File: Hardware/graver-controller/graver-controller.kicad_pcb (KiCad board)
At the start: 2 copper layers, 110 x 70 mm, 117 parts, among them J101 DC jack 5.5x2.1, J201 Handpiece, J301 USB-C, J302 SWD, J401 LCD XH 1x7, J402 NMJ6HCD2, Q101 DMP6023LE, Q201 IRLR3410, Q202 SI2309CDS, Q203 BSS123, SW301 BOOT0, SW302 RESET, SW401 EC11E15244G1, U101 LM5164DDAR, U102 AP2112K-3.3, U201 UCC27517DBVR, U202 TLV9062IDR, U301 STM32F411CEU6, U302 USBLC6-2SC6, U401 PESD5V0S2BT, Y301 25MHz 10pF

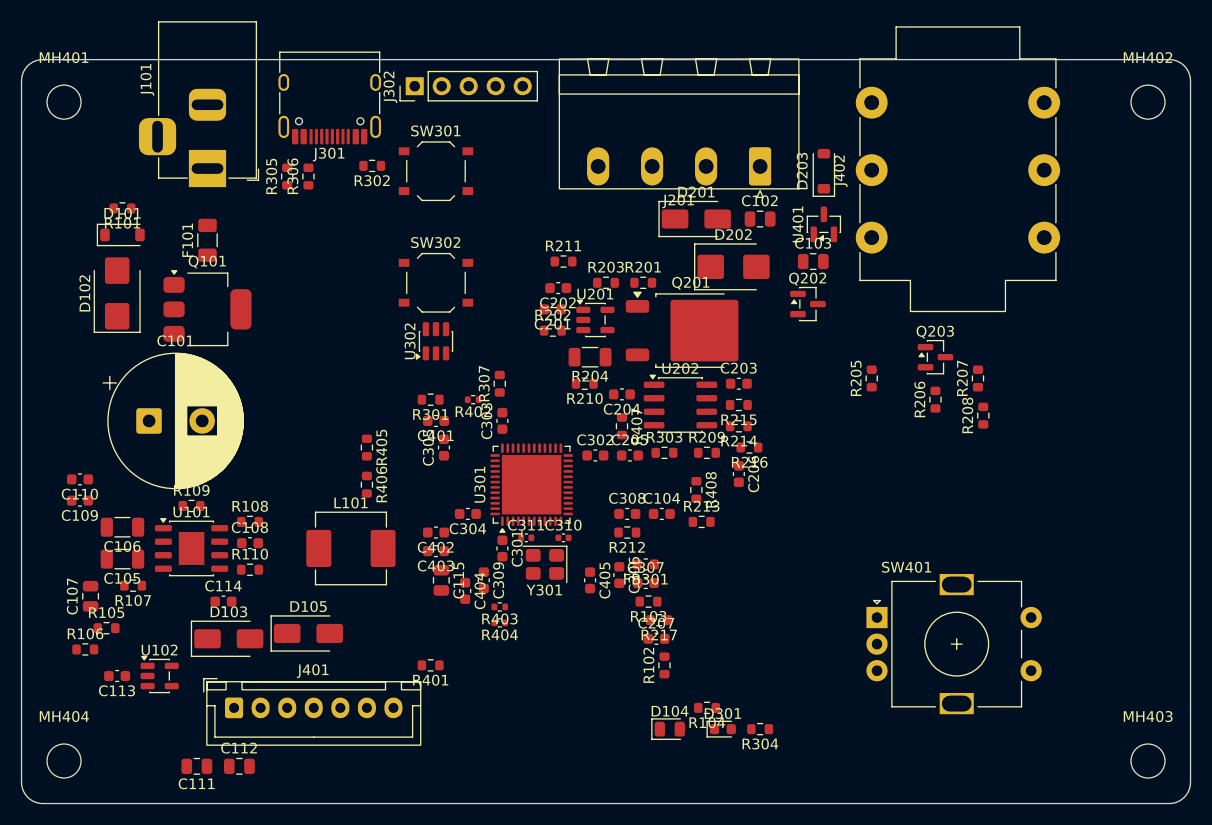
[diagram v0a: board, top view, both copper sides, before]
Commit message: hardware: copper script, first pass of the locked critical copper
tools/pcb/copper.py (place.py --copper): B.Cu ground pour, M3 and crystal
keepouts, QFN fanout with EP vias, decoupling links, crystal legs and
guard, VDDA chain, USB pair (39.8 / 39.0 mm, skew 0.8 mm, no vias),
VIN and flyback loop at 1.0 mm, buck loops, +5V / +3V3 links; all locked
and grouped. Repo board: 0 DRC errors, 0 parity, 107 pad pairs left for
the router. Known: NRST and the pedal inputs are trapped behind the
crystal island, R209/R213 are not at the shunt, 12 short local traces
not drawn; see README.
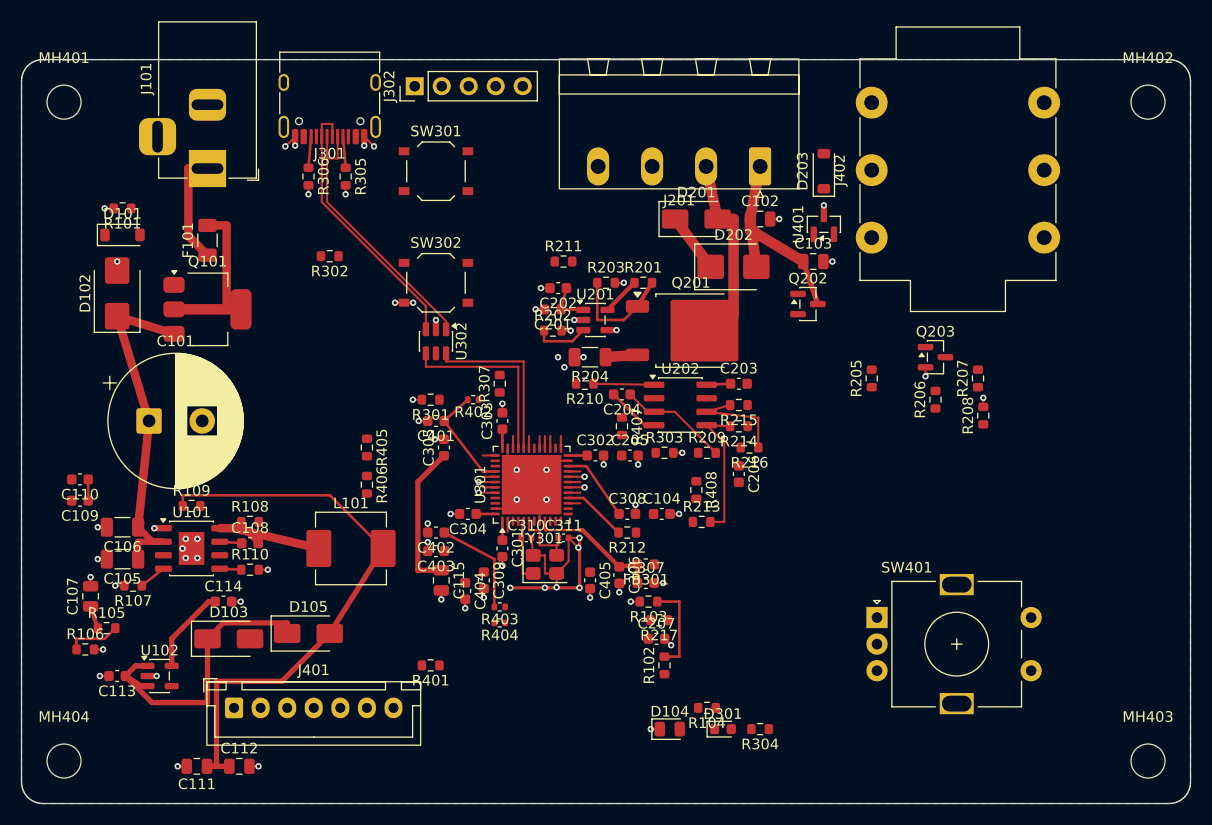
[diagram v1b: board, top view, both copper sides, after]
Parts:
- moved R302 9.39 mm to (79.0, 68.5)
- moved R305 5.50 mm to (80.5, 61.0), turned to -90 degrees
- moved C310 3.50 mm to (97.5, 95.0)
- moved C311 3.50 mm to (101.0, 95.0)
- turned R306 to -90 degrees
- turned U302 to -90 degrees
- turned Y301 to 0 degrees
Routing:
- net GND: track 0.00 -> 82.0 mm, vias 0 -> 74
- net VIN: track 0.00 -> 55.7 mm
- net Net-(D105-A): track 0.00 -> 54.9 mm
- net /MCU/USB_DP: track 0.00 -> 43.2 mm
- net /MCU/USB_DM: track 0.00 -> 42.0 mm
- net +5V: track 0.00 -> 32.9 mm
- net +3V3: track 0.00 -> 31.5 mm
- net Net-(Q101-D): track 0.00 -> 21.0 mm
- net /Driver/COIL_NEG: track 0.00 -> 15.6 mm
- net Net-(U101-SW): track 0.00 -> 13.8 mm
- net Net-(U202B-+): track 0.00 -> 13.3 mm
- net /MCU/VDDA: track 0.00 -> 12.7 mm
- net ENC_A: track 0.00 -> 11.3 mm
- net ENC_B: track 0.00 -> 11.0 mm
- net Net-(F101-Pad1): track 0.00 -> 10.7 mm
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- added copper zone on B.Cu, net GND

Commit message: hardware: copper pass 2, crystal in the corner, Kelvin taps at the shunt
Crystal island moved in front of pads 1-5 (PC13-15 unused): OSC legs
3.2 / 4.8 mm, pads 7-12 now escape freely, NRST cap 2.1 mm and VDDA 1 uF
2.5 mm from their pins. R209/R213 within 1.2 mm of the shunt pad edges,
Kelvin traces from the pad edges. Sense-side ground checked as a tree
with one tie at R204's ground pad, 5/5 pass. USB pair 37.9 / 37.9 mm,
skew 0. Repo board 0 DRC errors, 0 parity, 101 pad pairs left for the
router (was 107); strict routability test 6 open nets, 120 vias.
Known: VBAT decap 2.9 mm (advisory), R213 -> U202.5 and the buck
EN/UVLO divider left to the router, 12 local traces listed in README.
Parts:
- moved R405 31.3 mm to (113.5, 90.5)
- moved R406 31.3 mm to (113.5, 94.0)
- moved C110 27.0 mm to (82.5, 88.5), turned to 0 degrees
- moved C109 25.0 mm to (80.5, 90.5), turned to 0 degrees
- moved R211 21.1 mm to (109.0, 88.5), turned to -90 degrees
- moved R301 21.1 mm to (87.0, 103.0)
- moved R403 17.6 mm to (90.5, 84.5)
- moved R213 16.1 mm to (103.5, 81.2), turned to -90 degrees
- moved C205 15.8 mm to (104.2, 102.8)
- moved C207 14.0 mm to (105.2, 91.2)
- moved C311 11.1 mm to (94.9, 104.2), turned to -90 degrees
- moved R109 11.0 mm to (73.0, 100.5), turned to 180 degrees
- moved R209 10.7 mm to (106.0, 80.5)
- moved C404 8.96 mm to (100.0, 103.5)
- moved C402 8.49 mm to (87.0, 86.2)
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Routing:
- net GND: track 82.0 -> 119.1 mm, vias 74 -> 73
- net Net-(U202A--): track 0.00 -> 14.8 mm
- net Net-(U202B-+): track 13.3 -> 2.20 mm
- net Net-(D105-A): track 54.9 -> 44.1 mm
- net /Driver/OC_REF: track 9.97 -> 19.2 mm
- net /MCU/VDDA: track 12.7 -> 3.73 mm
- net VIN_SENSE: track 10.2 -> 1.55 mm
- net Net-(U301-VCAP1): track 7.16 -> 0.00 mm
- net ENC_A: track 11.3 -> 4.13 mm
- net ENC_B: track 11.0 -> 3.97 mm
- net I_SENSE: track 7.22 -> 1.15 mm
- net Net-(U301-PA10): track 1.15 -> 7.14 mm
- net LED_STAT: track 1.00 -> 6.56 mm, vias 0 -> 1
- net /Driver/SHUNT_HI: track 3.01 -> 8.35 mm
- net +3V3: track 31.5 -> 28.0 mm
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
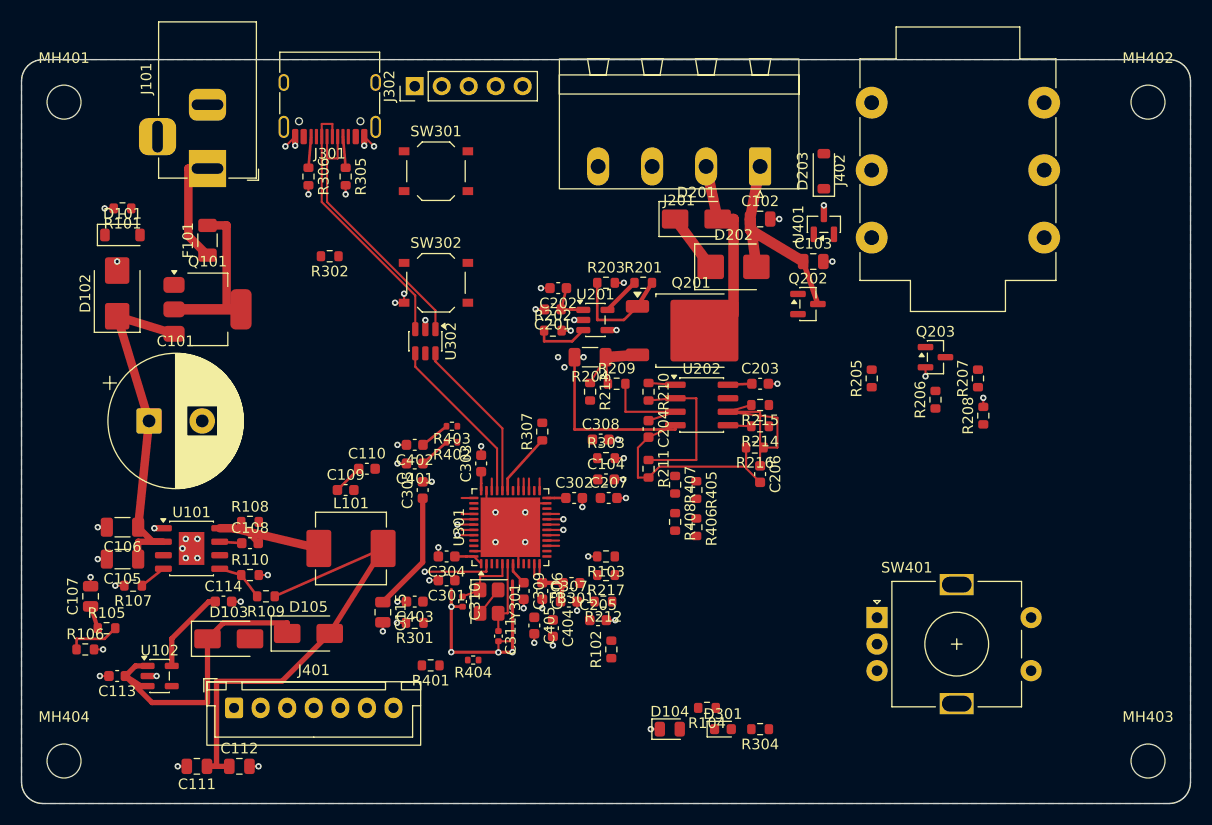
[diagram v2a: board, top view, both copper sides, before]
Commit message: hardware: scripted silkscreen
tools/pcb/silk.py (place.py --copper --silk): references at 1.0 mm /
0.15 mm placed by search next to their part, off pads and off each
other (10 inside the body, 87 within 1.5 mm, 7 within 3 mm, 9 in
reference rows); rear-edge labels DC 24V, USB, SWD, HANDPIECE with the
pins in board order (4 GND 3 NTC 2 COIL 1 VIN), PEDAL; J401 pin names;
pin-1 marks on J201, J302, J401; title. Library silk of the four rear
connectors clipped to the outline (4 lib_footprint_mismatch warnings,
deliberate). silk_overlap / silk_over_copper / silk_edge_clearance
92 / 92 / 17 -> 0. Copper unchanged (234 tracks, 78 vias, 6 zones),
0 DRC errors, 0 parity, 101 pad pairs left for the router.
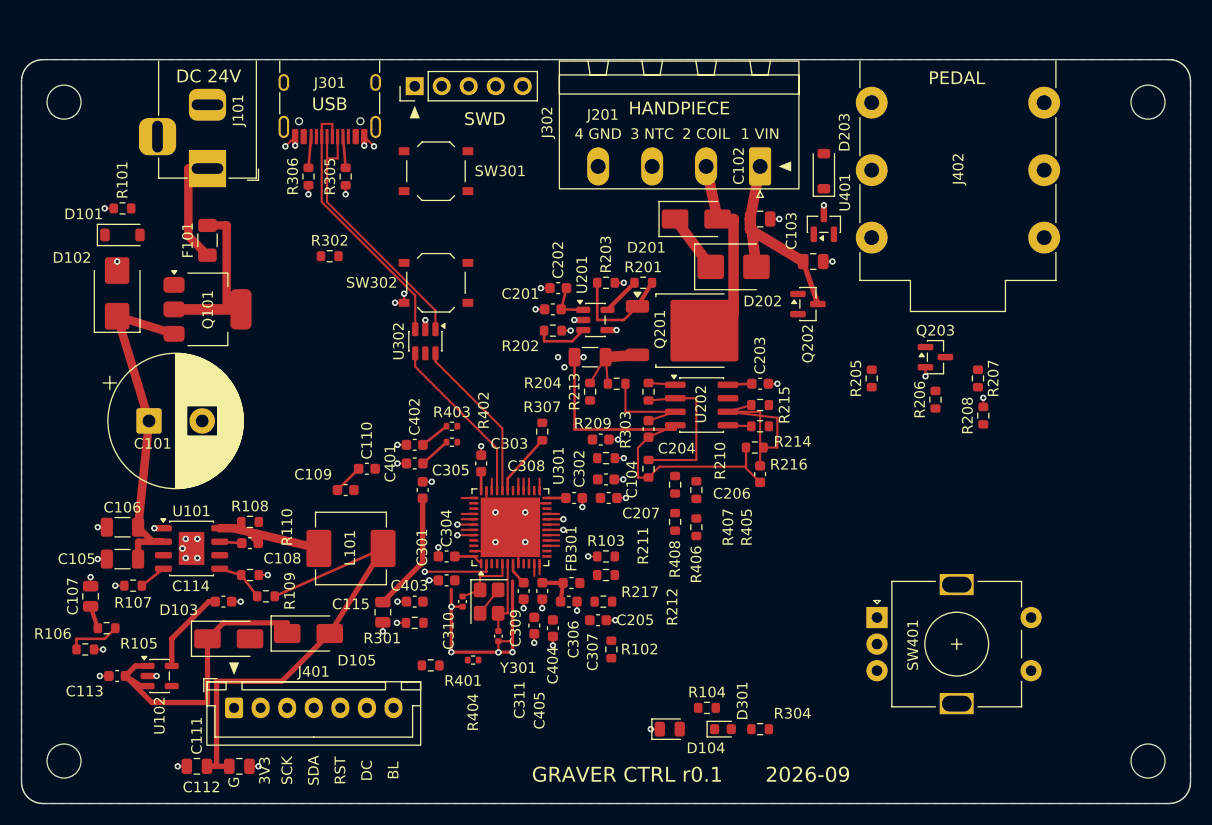
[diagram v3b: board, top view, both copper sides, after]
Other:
- board text added: "1 VIN"
- board text added: "2 COIL"
- board text added: "2026-09"
- board text added: "3 NTC"
- board text added: "3V3"
- board text added: "4 GND"
- board text added: "BL"
- board text added: "DC"
- board text added: "DC 24V"
- board text added: "G"
- board text added: "GRAVER CTRL r0.1"
- board text added: "HANDPIECE"
- board text added: "PEDAL"
- board text added: "RST"
- board text added: "SCK"
- board text added: "SDA"
- board text added: "SWD"
- board text added: "USB"

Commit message: hardware: autoroute stage for the remaining nets, first mostly routed board
tools/pcb/autoroute.py (place.py --route): copies the board to scratch,
runs KiCadRoutingTools with escalation off and strict sizes, grades the
copy with kicad-cli against the committed .kicad_pro and imports only
complete, error-free nets, grouped 'autorouted' so the stage can redo
them; zones refilled in pcbnew afterwards. copper.py reserves bands
along the USB pair on B.Cu after the router cut its ground reference
11 times. Scripted copper unchanged (234 tracks, 78 vias, flyback
20.3 mm, USB 37.88/37.88, Kelvin 1.15/1.23, sense ground 5/5).

Repo board: 0 DRC errors, 0 parity, 20 unconnected pad pairs in this
regeneration (the worker's run reached 13: the router is not
deterministic between runs). Left open: NTC, ENC_SW, ENC_B, +5V,
LCD_RST at the QFN (fanout stubs and vias boxing each other in at
0.5 mm pitch), the USBLC6 duplicate I/O pins (need two short bridges),
the encoder's two MP lugs. Ugly: +3V3 runs 229 mm, CLAMP tap 50 mm
around the DPAK.
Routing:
- net +3V3: track 28.0 -> 226.1 mm, vias 0 -> 17
- net VIN: track 55.7 -> 198.0 mm, vias 0 -> 2
- net VBUS: track 0.00 -> 74.6 mm, vias 0 -> 6
- net ENC_A: track 4.13 -> 72.2 mm, vias 0 -> 5
- net /Driver/CLAMP: track 5.61 -> 73.5 mm, vias 0 -> 2
- net SWDIO: track 1.15 -> 64.0 mm, vias 0 -> 2
- net NRST: track 2.18 -> 58.1 mm, vias 0 -> 4
- net LED_STAT: track 6.56 -> 54.3 mm, vias 1 -> 6
- net Net-(U301-BOOT0): track 1.55 -> 47.1 mm, vias 1 -> 3
- net LCD_DC: track 1.15 -> 46.4 mm, vias 0 -> 4
- net Net-(D203-A): track 0.00 -> 43.2 mm
- net Net-(U401-A2): track 0.00 -> 43.1 mm, vias 0 -> 7
- net Net-(U401-A1): track 0.00 -> 42.9 mm, vias 0 -> 5
- net OC_TRIP: track 1.15 -> 42.1 mm, vias 0 -> 2
- net LCD_MOSI: track 1.15 -> 41.8 mm, vias 0 -> 3
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
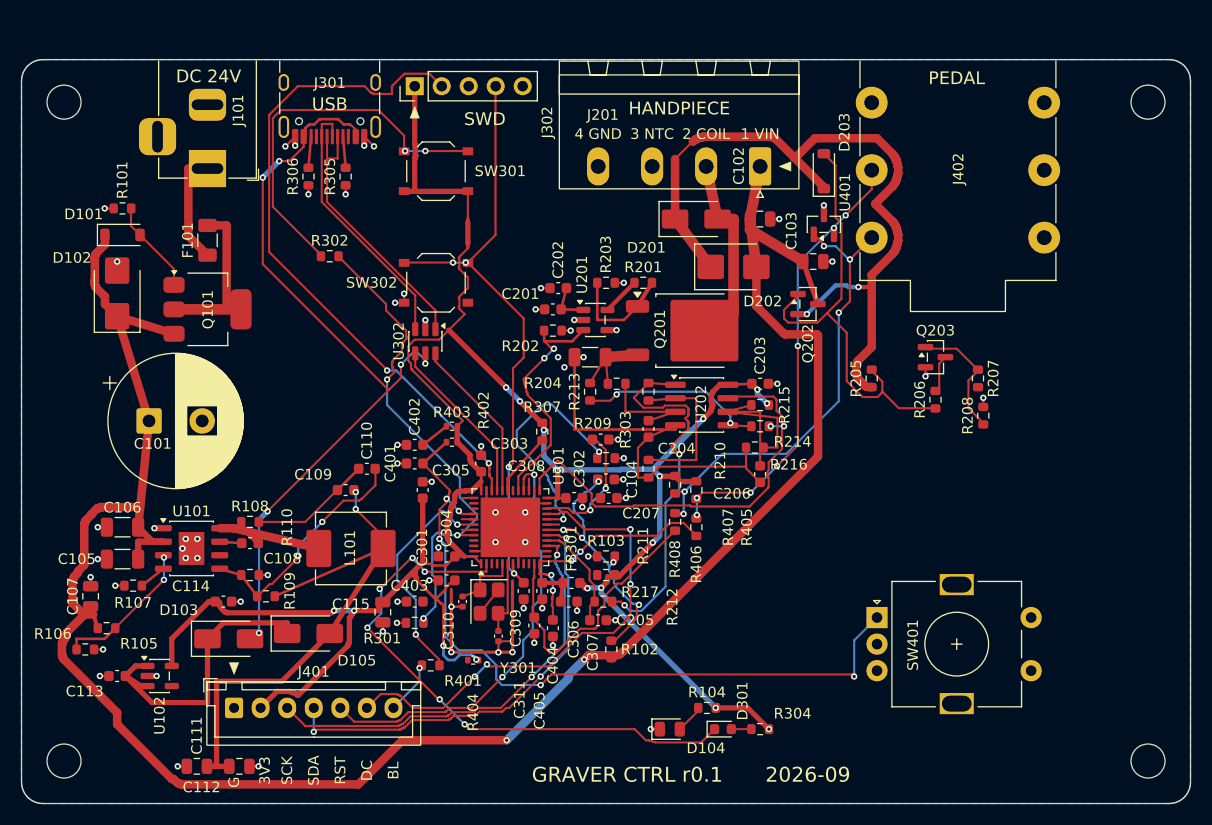
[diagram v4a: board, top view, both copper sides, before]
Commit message: hardware: QFN escape fan, scripted 3V3 trunk and CLAMP tap, 6 pad pairs left
copper.py: QFN pads 15-21 and 40-44 escape as a 45-degree fan into a
second ring with the vias at 2.9 mm, so no pad is boxed in any more;
USBLC6 die-duplicate pins bridged (1+6, 3+4); encoder MP lugs linked;
+3V3 as a scripted tree (240 mm, 0 vias; the MST floor over its 29 pads
is 183 mm, the ADR's 120 mm budget is not reachable with this placement);
+5V 33 mm, no via; CLAMP D202 -> Q202 tap 12.7 mm instead of the
router's 50 mm. autoroute.py runs the router three times and imports
the best (fewest errors, open, vias); summary in output/pcb.

Repo board: 0 DRC errors, 0 parity, 6 unconnected pad pairs
(VIN_SENSE x3, +5V, GATE_IN, VCAP1), 213 vias. Budgets: USB
37.88/37.88 skew 0, flyback 21.4 mm (was 20.3), Kelvin 1.15/1.23,
sense ground 5/5, no ADC net parallel to a switching net, nothing in
the M3 or crystal keepouts. Ugly: +3V3 278 mm total, ENC_B 106 mm,
NRST 88 mm; the right third of the board is still empty.
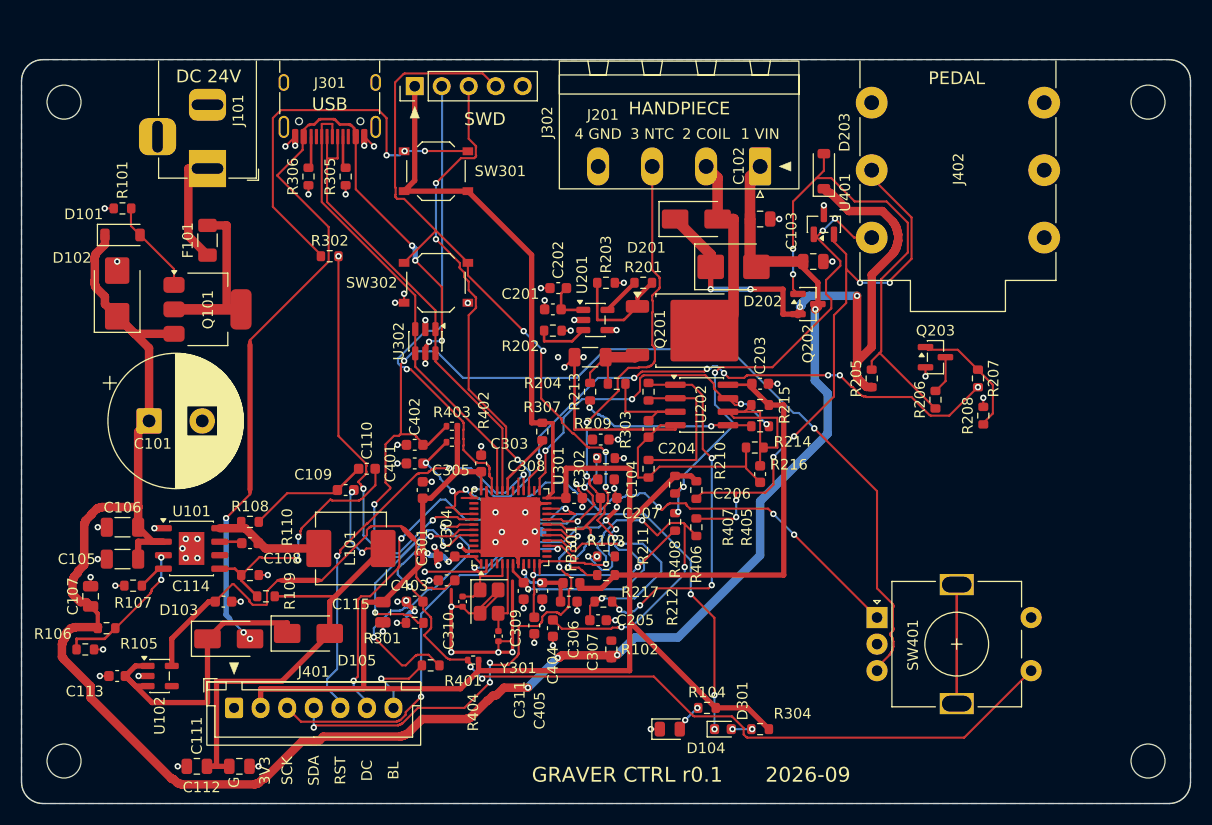
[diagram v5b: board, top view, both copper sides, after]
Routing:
- net ENC_B: track 3.97 -> 106.4 mm, vias 0 -> 4
- net ENC_SW: track 1.15 -> 81.5 mm, vias 0 -> 4
- net GND: track 119.1 -> 193.6 mm, vias 73 -> 84
- net +3V3: track 226.1 -> 277.9 mm, vias 17 -> 2
- net DECAY_SLOW: track 1.15 -> 52.4 mm, vias 0 -> 7
- net SWCLK: track 1.15 -> 52.2 mm, vias 0 -> 4
- net NTC: track 1.15 -> 51.7 mm, vias 0 -> 4
- net NRST: track 58.1 -> 87.8 mm, vias 4 -> 6
- net VIN_SENSE: track 25.2 -> 3.15 mm, vias 5 -> 1
- net SWDIO: track 64.0 -> 45.0 mm, vias 2 -> 1
- net PEDAL_RING: track 23.4 -> 41.3 mm
- net GATE_IN: track 23.2 -> 6.27 mm, vias 2 -> 0
- net /Driver/CLAMP: track 73.5 -> 57.9 mm, vias 2 -> 4
- net VBUS: track 74.6 -> 89.6 mm, vias 6 -> 8
- net Net-(U401-A2): track 43.1 -> 57.7 mm, vias 7 -> 6
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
